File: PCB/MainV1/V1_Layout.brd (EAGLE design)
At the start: 50.1 x 73.7 mm, 47 parts, among them IC1 LM6482, IC2 AD623N, U2 MB85RC256VPF-G-JNERE2

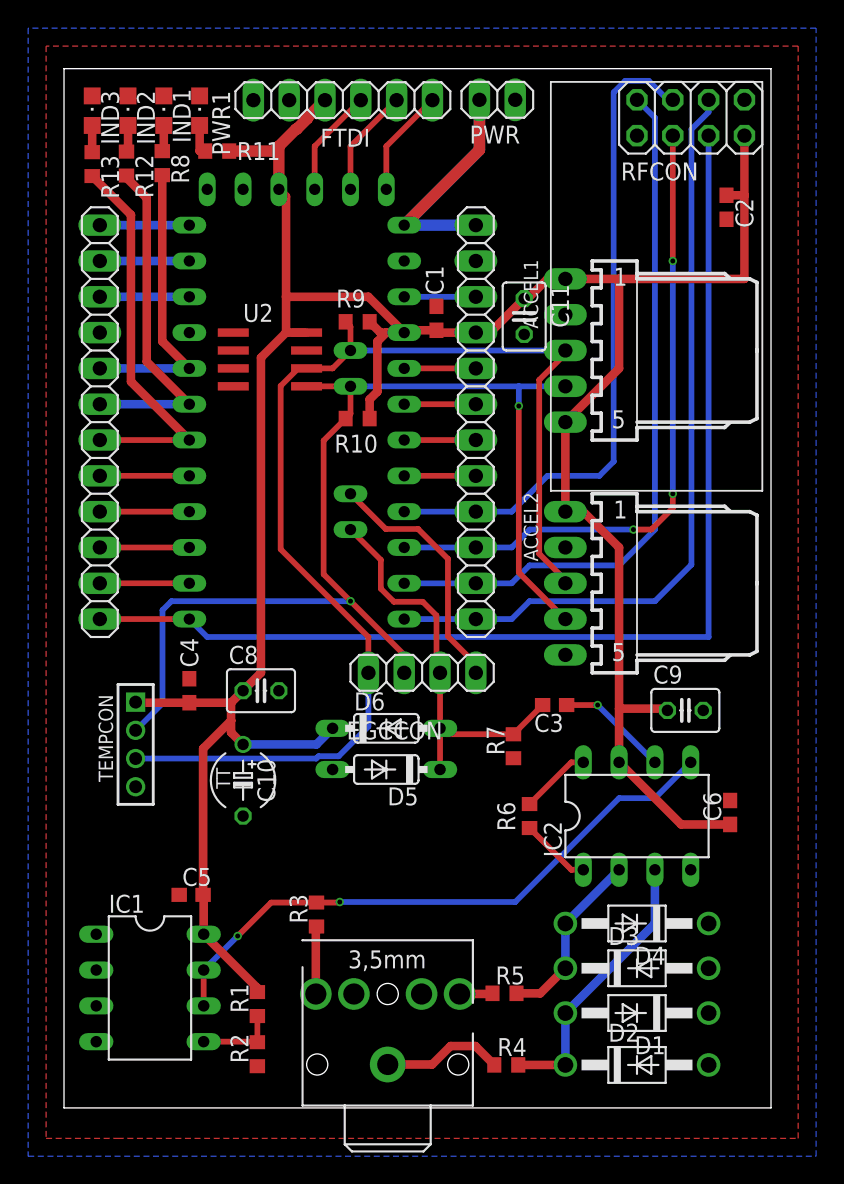
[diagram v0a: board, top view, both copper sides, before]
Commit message: Reviewed layout, added text, rounded corners. Design rule check passed. Ready for final review
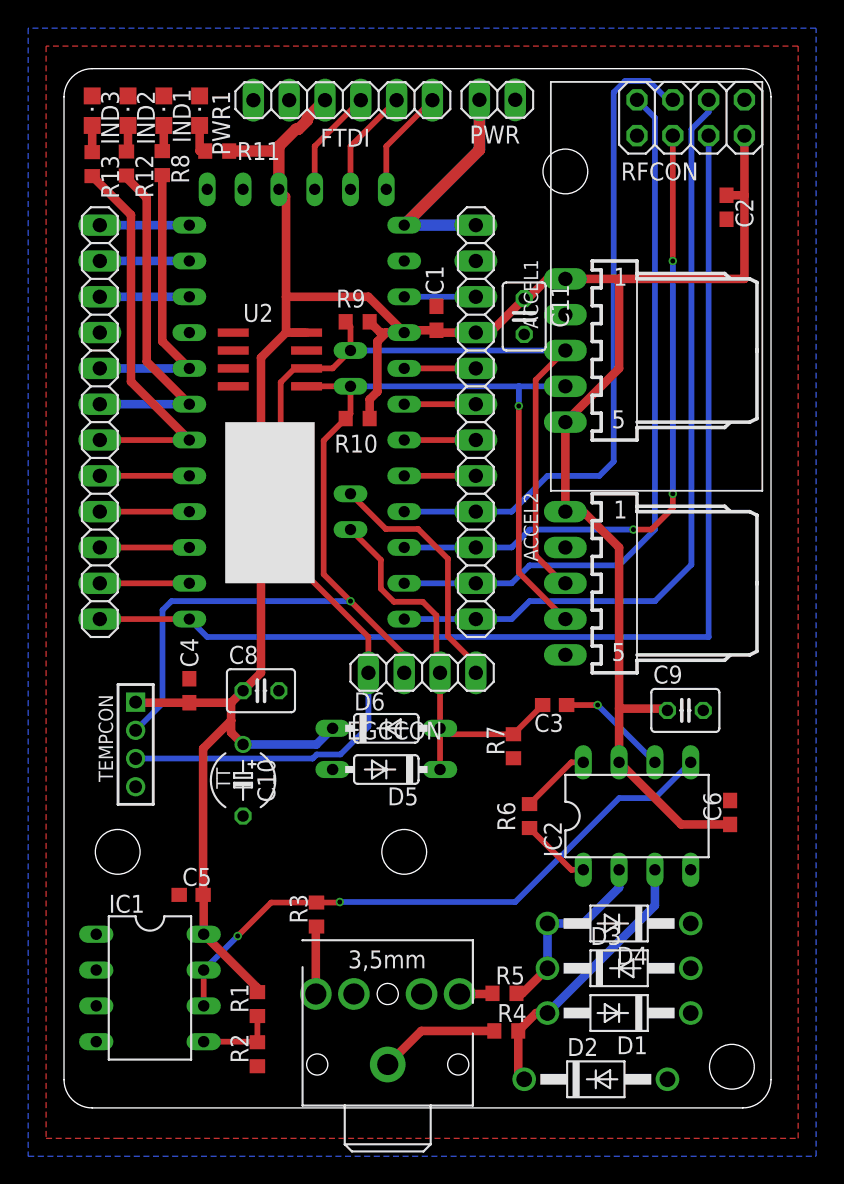
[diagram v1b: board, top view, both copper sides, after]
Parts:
- moved D2 3.09 mm to (54.2, 16.9)
- moved R4 2.41 mm to (47.9, 20.3)
- moved D1 1.27 mm to (55.9, 21.6)
- moved D3 1.27 mm to (55.9, 24.8)
- moved D4 1.27 mm to (55.9, 27.9)
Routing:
- net N$2: track 12.8 -> 13.5 mm
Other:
- outline, holes or cut-outs redrawn
- board text added: "Designed by Nicolas Weninger"
- board text added: "ES96"
- board text added: "Main Board V1"

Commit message: Ordered. Added CAM files. Added 3D desgn files for Fusion 360.
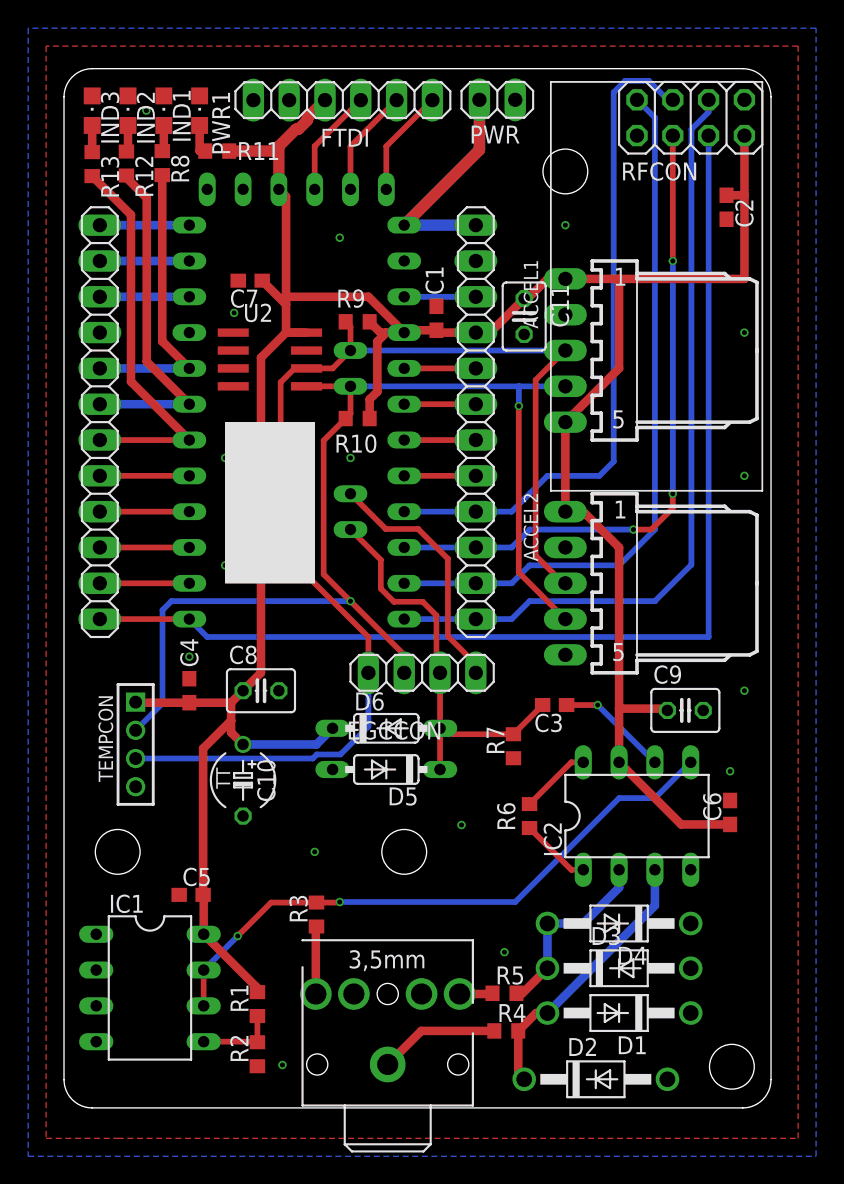
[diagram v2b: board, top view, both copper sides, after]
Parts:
- added C7: 1uF, rcl:C0603
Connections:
- net +3V3: now also C7.1
- net GND: now also C7.2
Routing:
- net +3V3: track 197.2 -> 199.6 mm
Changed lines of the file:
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@@
 </layers>
 <board>
+<fusionsync huburn="a.cGVyc29uYWw6dWUyYTQwNWMw" projecturn="a.cGVyc29uYWw6dWUyYTQwNWMwIzIwMTgxMTIyMTYxNjk0NTgx" f3durn="urn:adsk.wipprod:dm.lineage:MMUmWtWFTf6voOu1sfa3kA" pcbguid="9e39180f-c811-4b1d-9b29-3bf5fe3fa75b" lastpulledtime="" lastsyncedchangeguid="81426712-97eb-26f6-5639-6a3e30396f2e"/>
 <plain>
 <wire x1="16.51" y1="86.57" x2="16.51" y2="16.859" width="0" layer="20"/>
@@
 <text x="62.23" y="62.23" size="2.54" layer="22" rot="MR270" align="center">Designed by
 Nicolas Weninger</text>
+<rectangle x1="27.94" y1="52.07" x2="34.29" y2="63.5" layer="21"/>
+<dimension x1="18.51" y1="88.57" x2="18.51" y2="14.859" x3="8.89" y3="51.7145" textsize="1.778" layer="51"/>
+<dimension x1="16.51" y1="86.57" x2="66.655" y2="86.57" x3="41.5825" y3="95.25" textsize="1.778" layer="51"/>
 </plain>
 <attributes>
@@
 <attribute name="SPICEPREFIX" value="C" x="29.21" y="38.1" size="1.778" layer="27" rot="R270" display="off"/>
 </element>
+<element name="C7" library="rcl" library_urn="urn:adsk.eagle:library:334" package="C0603" package3d_urn="urn:adsk.eagle:package:23616/2" value="1uF" x="29.718" y="73.533" smashed="yes" rot="R180">
+<attribute name="NAME" x="30.353" y="72.898" size="1.27" layer="25" rot="R180"/>
+<attribute name="SPICEPREFIX" value="C" x="29.718" y="73.533" size="1.778" layer="27" rot="R180" display="off"/>
+</element>
 </elements>
 <signals>
@@
 <contactref element="D2" pad="A"/>
 <contactref element="D1" pad="C"/>
+<via x="52.07" y="77.47" extent="1-16" drill="0.35"/>
+<via x="34.29" y="33.02" extent="1-16" drill="0.35"/>
+<via x="27.94" y="53.34" extent="1-16" drill="0.35"/>
+<via x="27.94" y="60.96" extent="1-16" drill="0.35"/>
+<via x="22.352" y="85.598" extent="1-16" drill="0.35"/>
+<via x="47.752" y="25.908" extent="1-16" drill="0.35"/>
+<via x="63.754" y="38.735" extent="1-16" drill="0.35"/>
+<via x="28.575" y="71.247" extent="1-16" drill="0.35"/>
+<contactref element="C7" pad="2"/>
+<via x="25.4" y="46.863" extent="1-16" drill="0.35"/>
+<via x="32.004" y="17.907" extent="1-16" drill="0.35"/>
+<via x="64.77" y="69.85" extent="1-16" drill="0.35"/>
+<via x="64.77" y="59.69" extent="1-16" drill="0.35"/>
+<via x="64.77" y="44.45" extent="1-16" drill="0.35"/>
+<via x="44.704" y="34.925" extent="1-16" drill="0.35"/>
+<via x="36.83" y="60.96" extent="1-16" drill="0.35"/>
+<via x="36.068" y="76.581" extent="1-16" drill="0.35"/>
 </signal>
 <signal name="N$2">
@@
 <wire x1="31.75" y1="80.01" x2="32.258" y2="79.502" width="0.6096" layer="1"/>
 <wire x1="32.258" y1="79.502" x2="32.258" y2="72.39" width="0.6096" layer="1"/>
-<wire x1="32.258" y1="72.39" x2="32.258" y2="69.85" width="0.6096" layer="1"/>
+<wire x1="32.258" y1="72.39" x2="32.258" y2="71.843" width="0.6096" layer="1"/>
 <wire x1="32.258" y1="69.85" x2="33.715" y2="69.85" width="0.6096" layer="1"/>
 <wire x1="45.72" y1="69.85" x2="43.092" y2="69.85" width="0.6096" layer="1"/>
@@
 <wire x1="26.416" y1="27.178" x2="30.226" y2="23.368" width="0.6096" layer="1"/>
 <wire x1="30.226" y1="23.368" x2="30.226" y2="23.075" width="0.6096" layer="1"/>
+<contactref element="C7" pad="1"/>
+<wire x1="30.568" y1="73.533" x2="32.258" y2="71.843" width="0.6096" layer="1"/>
+<wire x1="32.258" y1="71.843" x2="32.258" y2="69.85" width="0.6096" layer="1"/>
 </signal>
 <signal name="D10">
@@
 </note>
 <note version="8.3" severity="warning">
+Since Version 8.3, EAGLE supports Fusion synchronisation.
+This feature will not be available in this version and saving
+the document will break the link to the Fusion PCB feature.
+</note>
+<note version="8.3" severity="warning">

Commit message: Added comments in schematc
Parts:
- R3: value 330k -> 0R
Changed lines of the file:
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@@
 <attribute name="SPICEPREFIX" value="R" x="111.506" y="55.499" size="1.778" layer="27" rot="R90" display="off"/>
 </element>
-<element name="R3" library="rcl" library_urn="urn:adsk.eagle:library:334" package="R0603" package3d_urn="urn:adsk.eagle:package:23555/2" value="330k" x="34.417" y="28.575" smashed="yes" rot="R90">
+<element name="R3" library="rcl" library_urn="urn:adsk.eagle:library:334" package="R0603" package3d_urn="urn:adsk.eagle:package:23555/2" value="0R" x="34.417" y="28.575" smashed="yes" rot="R90">
 <attribute name="NAME" x="33.782" y="27.94" size="1.27" layer="25" rot="R90"/>
 <attribute name="SPICEPREFIX" value="R" x="115.697" y="71.755" size="1.778" layer="27" rot="R90" display="off"/>
